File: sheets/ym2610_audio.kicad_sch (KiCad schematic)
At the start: 55 parts, among them J3 SMK S-G8043, Q101 2SC1815, Q102 2SC1815, U26 YM3016D, U27 YM2610, U28 PC4741, U29 PC4741

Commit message: Sync footprints from Nightly Build
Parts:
- C11, C12, C2, C301, C4, C5, C6, C7, C8: footprint 1_NeoGeoLibrary:CAP1-5mm -> 1_NeoGeoLibrary:CAP2-2.5mm
- C24, C25: footprint 1_NeoGeoLibrary:CAP3-5mm -> 1_NeoGeoLibrary:CAP2-2.5mm
- Q101, Q102: footprint Package_TO_SOT_THT:TO-92_Inline -> Package_TO_SOT_THT:TO-92_Inline_Wide
- R33, R34: footprint 1_NeoGeoLibrary:Resistor1-5mm -> Resistor_THT:R_Axial_DIN0207_L6.3mm_D2.5mm_P10.16mm_Horizontal
- U27: footprint Package_DIP:DIP-64_W25.4mm -> 1_NeoGeoLibrary:68000
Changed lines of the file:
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@@
     (property "Reference" "C4" (id 0) (at 105.664 221.107 90))
     (property "Value" "10uF" (id 1) (at 105.918 222.885 90))
-    (property "Footprint" "1_NeoGeoLibrary:CAP1-5mm" (id 2) (at 105.791 217.678 0)
+    (property "Footprint" "1_NeoGeoLibrary:CAP2-2.5mm" (id 2) (at 105.791 217.678 0)
       (effects (font (size 1.27 1.27)) hide)
     )
@@
       (effects (font (size 1.27 1.27)) (justify right))
     )
-    (property "Footprint" "1_NeoGeoLibrary:CAP3-5mm" (id 2) (at 58.928 239.522 0)
+    (property "Footprint" "1_NeoGeoLibrary:CAP2-2.5mm" (id 2) (at 58.928 239.522 0)
       (effects (font (size 1.27 1.27)) hide)
     )
@@
       (effects (font (size 1.27 1.27)) (justify left))
     )
-    (property "Footprint" "Package_TO_SOT_THT:TO-92_Inline" (id 2) (at 185.293 210.058 0)
+    (property "Footprint" "Package_TO_SOT_THT:TO-92_Inline_Wide" (id 2) (at 185.293 210.058 0)
       (effects (font (size 1.27 1.27) italic) (justify left) hide)
     )
@@
       (effects (font (size 1.27 1.27)) (justify left))
     )
-    (property "Footprint" "Package_TO_SOT_THT:TO-92_Inline" (id 2) (at 185.293 225.298 0)
+    (property "Footprint" "Package_TO_SOT_THT:TO-92_Inline_Wide" (id 2) (at 185.293 225.298 0)
       (effects (font (size 1.27 1.27) italic) (justify left) hide)
     )
@@
     (property "Reference" "C8" (id 0) (at 232.029 232.918 90))
     (property "Value" "10uF" (id 1) (at 232.029 234.696 90))
-    (property "Footprint" "1_NeoGeoLibrary:CAP1-5mm" (id 2) (at 232.029 230.378 0)
+    (property "Footprint" "1_NeoGeoLibrary:CAP2-2.5mm" (id 2) (at 232.029 230.378 0)
       (effects (font (size 1.27 1.27)) hide)
     )
@@
       (effects (font (size 1.27 1.27)) (justify left))
     )
-    (property "Footprint" "1_NeoGeoLibrary:CAP1-5mm" (id 2) (at 186.182 56.261 0)
+    (property "Footprint" "1_NeoGeoLibrary:CAP2-2.5mm" (id 2) (at 186.182 56.261 0)
       (effects (font (size 1.27 1.27)) hide)
     )
@@
     (property "Reference" "R33" (id 0) (at 239.776 221.869 90))
     (property "Value" "10Ω" (id 1) (at 239.776 224.409 90))
-    (property "Footprint" "1_NeoGeoLibrary:Resistor1-5mm" (id 2) (at 239.776 226.568 0)
+    (property "Footprint" "Resistor_THT:R_Axial_DIN0207_L6.3mm_D2.5mm_P10.16mm_Horizontal" (id 2) (at 239.776 226.568 0)
       (effects (font (size 1.27 1.27)) hide)
     )
@@
     (property "Reference" "C11" (id 0) (at 117.094 252.73 90))
     (property "Value" "10uF" (id 1) (at 117.348 254.508 90))
-    (property "Footprint" "1_NeoGeoLibrary:CAP1-5mm" (id 2) (at 117.221 249.301 0)
+    (property "Footprint" "1_NeoGeoLibrary:CAP2-2.5mm" (id 2) (at 117.221 249.301 0)
       (effects (font (size 1.27 1.27)) hide)
     )
@@
     (property "Reference" "R34" (id 0) (at 239.776 213.487 90))
     (property "Value" "10Ω" (id 1) (at 239.776 210.947 90))
-    (property "Footprint" "1_NeoGeoLibrary:Resistor1-5mm" (id 2) (at 239.776 208.788 0)
+    (property "Footprint" "Resistor_THT:R_Axial_DIN0207_L6.3mm_D2.5mm_P10.16mm_Horizontal" (id 2) (at 239.776 208.788 0)
       (effects (font (size 1.27 1.27)) hide)
     )
@@
     (property "Reference" "C12" (id 0) (at 117.221 181.102 90))
     (property "Value" "10uF" (id 1) (at 117.221 183.134 90))
-    (property "Footprint" "1_NeoGeoLibrary:CAP1-5mm" (id 2) (at 117.221 186.055 0)
+    (property "Footprint" "1_NeoGeoLibrary:CAP2-2.5mm" (id 2) (at 117.221 186.055 0)
       (effects (font (size 1.27 1.27)) hide)
     )
@@
     (property "Reference" "C5" (id 0) (at 186.944 197.231 0))
     (property "Value" "10uF" (id 1) (at 187.071 199.009 0))
-    (property "Footprint" "1_NeoGeoLibrary:CAP1-5mm" (id 2) (at 182.753 197.993 0)
+    (property "Footprint" "1_NeoGeoLibrary:CAP2-2.5mm" (id 2) (at 182.753 197.993 0)
       (effects (font (size 1.27 1.27)) hide)
     )
@@
       (effects (font (size 1.27 1.27)) (justify right))
     )
-    (property "Footprint" "1_NeoGeoLibrary:CAP1-5mm" (id 2) (at 233.426 50.546 0)
+    (property "Footprint" "1_NeoGeoLibrary:CAP2-2.5mm" (id 2) (at 233.426 50.546 0)
       (effects (font (size 1.27 1.27)) hide)
     )
@@
     (property "Reference" "C6" (id 0) (at 187.198 236.474 0))
     (property "Value" "10uF" (id 1) (at 187.198 238.252 0))
-    (property "Footprint" "1_NeoGeoLibrary:CAP1-5mm" (id 2) (at 182.753 237.363 0)
+    (property "Footprint" "1_NeoGeoLibrary:CAP2-2.5mm" (id 2) (at 182.753 237.363 0)
       (effects (font (size 1.27 1.27)) hide)
     )
@@
     (property "Reference" "U27" (id 0) (at 100.33 29.845 0))
     (property "Value" "YM2610" (id 1) (at 108.458 138.811 0))
-    (property "Footprint" "Package_DIP:DIP-64_W25.4mm" (id 2) (at 108.458 89.281 0)
+    (property "Footprint" "1_NeoGeoLibrary:68000" (id 2) (at 108.458 89.281 0)
       (effects (font (size 1.27 1.27)) hide)
     )
@@
     (property "Reference" "C7" (id 0) (at 232.029 200.66 90))
     (property "Value" "10uF" (id 1) (at 232.029 202.438 90))
-    (property "Footprint" "1_NeoGeoLibrary:CAP1-5mm" (id 2) (at 232.029 204.978 0)
+    (property "Footprint" "1_NeoGeoLibrary:CAP2-2.5mm" (id 2) (at 232.029 204.978 0)
       (effects (font (size 1.27 1.27)) hide)
     )
@@
       (effects (font (size 1.27 1.27)) (justify right))
     )
-    (property "Footprint" "1_NeoGeoLibrary:CAP3-5mm" (id 2) (at 58.928 195.834 0)
-      (effects (font (size 1.27 1.27)) hide)
-    )
+    (property "Footprint" "1_NeoGeoLibrary:CAP2-2.5mm" (id 2) (at 58.928 195.834 0)
+      (effects (font (size 1.27 1.27)) hide)
+    )

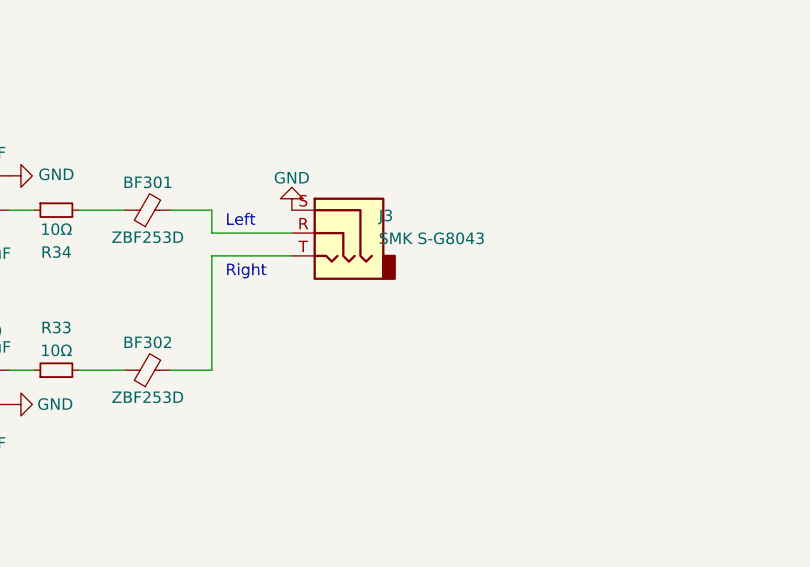
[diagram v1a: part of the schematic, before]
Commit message: 1. Swap Halt / Reset on RA1 2. Added more Power Caps 3. Change Audio socket Left/Right around 4. Added Ferrite Beads to Audio Signals 5. Added Ferrite Beads to Video Signals
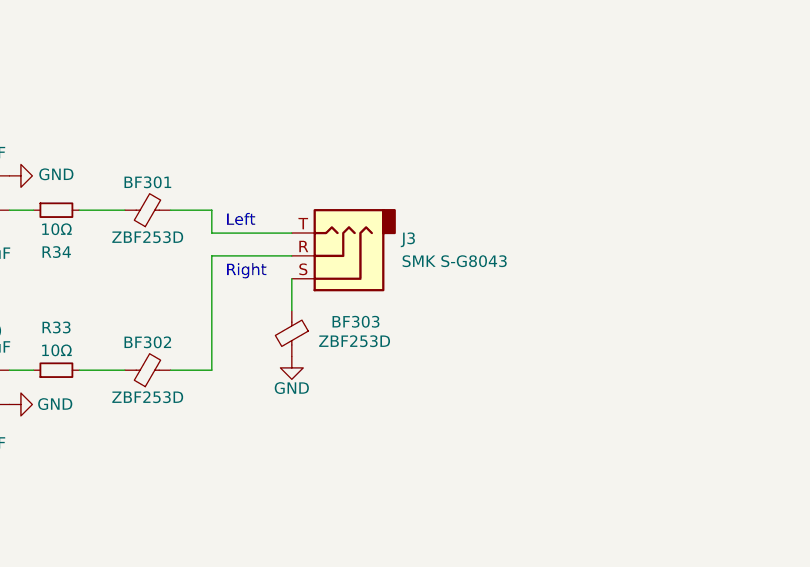
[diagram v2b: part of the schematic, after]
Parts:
- added BF303: ZBF253D, 1_NeoGeoLibrary:BF-2.5mm, symbol Device:FerriteBead_Small
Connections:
- net GND: now also BF303.2; no longer J3.S
- net at BF301.2: now also J3.T; no longer J3.R
- net at BF302.2: now also J3.R; no longer J3.T
- new net: BF303.1, J3.S
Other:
- moved on the sheet: J3
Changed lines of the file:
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@@
+    (stroke (width 0) (type default) (color 0 0 0 0))
+  )
+  (wire (pts (xy 265.938 216.408) (xy 265.938 219.964))
     (stroke (width 0) (type default) (color 0 0 0 0))
   )
@@
     (pin "2")
   )
+  (symbol (lib_id "Device:FerriteBead_Small") (at 265.938 222.504 0) (mirror y) (unit 1)
+    (in_bom yes) (on_board yes)
+    (property "Reference" "BF303" (id 0) (at 273.05 221.234 0))
+    (property "Value" "ZBF253D" (id 1) (at 272.923 223.393 0))
+    (property "Footprint" "1_NeoGeoLibrary:BF-2.5mm" (id 2) (at 267.716 222.504 90)
+      (effects (font (size 1.27 1.27)) hide)
+    )
+    (property "Datasheet" "" (id 3) (at 265.938 222.504 0)
+      (effects (font (size 1.27 1.27)) hide)
+    )
+    (pin "1")
+    (pin "2")
+  )
   (symbol (lib_id "Device:R_Small") (at 222.885 206.883 270) (mirror x) (unit 1)
     (in_bom yes) (on_board yes)
@@
     (pin "2")
   )
-  (symbol (lib_id "power:GND") (at 265.938 208.788 180) (unit 1)
-    (in_bom yes) (on_board yes)
-    (property "Reference" "#PWR0193" (id 0) (at 265.938 202.438 0)
-      (effects (font (size 1.27 1.27)) hide)
-    )
-    (property "Value" "GND" (id 1) (at 265.938 205.232 0))
-    (property "Footprint" "" (id 2) (at 265.938 208.788 0)
-      (effects (font (size 1.27 1.27)) hide)
-    )
-    (property "Datasheet" "" (id 3) (at 265.938 208.788 0)
+  (symbol (lib_id "power:GND") (at 265.938 225.044 0) (mirror y) (unit 1)
+    (in_bom yes) (on_board yes)
+    (property "Reference" "#PWR0193" (id 0) (at 265.938 231.394 0)
+      (effects (font (size 1.27 1.27)) hide)
+    )
+    (property "Value" "GND" (id 1) (at 265.938 228.6 0))
+    (property "Footprint" "" (id 2) (at 265.938 225.044 0)
+      (effects (font (size 1.27 1.27)) hide)
+    )
+    (property "Datasheet" "" (id 3) (at 265.938 225.044 0)
       (effects (font (size 1.27 1.27)) hide)
     )
@@
   (symbol (lib_id "power:GND") (at 58.928 252.095 0) (unit 1)
     (in_bom yes) (on_board yes)
-    (property "Reference" "#PWR?" (id 0) (at 58.928 258.445 0)
+    (property "Reference" "#PWR0199" (id 0) (at 58.928 258.445 0)
       (effects (font (size 1.27 1.27)) hide)
     )
@@
     (pin "2")
   )
-  (symbol (lib_id "Connector:AudioJack3") (at 271.018 211.328 0) (mirror y) (unit 1)
+  (symbol (lib_id "Connector:AudioJack3") (at 271.018 213.868 180) (unit 1)
     (in_bom yes) (on_board yes) (fields_autoplaced)
-    (property "Reference" "J3" (id 0) (at 275.59 209.4229 0)
+    (property "Reference" "J3" (id 0) (at 278.13 211.9629 0)
       (effects (font (size 1.27 1.27)) (justify right))
     )
-    (property "Value" "SMK S-G8043" (id 1) (at 275.59 211.9629 0)
+    (property "Value" "SMK S-G8043" (id 1) (at 278.13 214.5029 0)
       (effects (font (size 1.27 1.27)) (justify right))
     )
-    (property "Footprint" "Connector_Audio:Jack_3.5mm_CUI_SJ1-3523N_Horizontal" (id 2) (at 271.018 211.328 0)
-      (effects (font (size 1.27 1.27)) hide)
-    )
-    (property "Datasheet" "~" (id 3) (at 271.018 211.328 0)
+    (property "Footprint" "Connector_Audio:Jack_3.5mm_CUI_SJ1-3523N_Horizontal" (id 2) (at 271.018 213.868 0)
+      (effects (font (size 1.27 1.27)) hide)
+    )
+    (property "Datasheet" "~" (id 3) (at 271.018 213.868 0)
       (effects (font (size 1.27 1.27)) hide)
     )
@@
   (symbol (lib_id "power:GND") (at 58.928 183.261 180) (unit 1)
     (in_bom yes) (on_board yes)
-    (property "Reference" "#PWR?" (id 0) (at 58.928 176.911 0)
-      (effects (font (size 1.27 1.27)) hide)
-    )
+    (property "Reference" "#PWR0200" (id 0) (at 58.928 176.911 0)
+      (effects (font (size 1.27 1.27)) hide)
+    )

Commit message: Sync Footprints from Nightly
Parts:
- J3: footprint Connector_Audio:Jack_3.5mm_CUI_SJ1-3523N_Horizontal -> 1_NeoGeoLibrary:J3
- Q101, Q102: footprint Package_TO_SOT_THT:TO-92_Inline_Wide -> 1_NeoGeoLibrary:Transistor
- RV1: footprint Connector_PinHeader_2.54mm:PinHeader_1x06_P2.54mm_Vertical -> 1_NeoGeoLibrary:Volume-Slider
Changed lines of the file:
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@@
       (effects (font (size 1.27 1.27)) (justify left))
     )
-    (property "Footprint" "Package_TO_SOT_THT:TO-92_Inline_Wide" (id 2) (at 185.293 210.058 0)
+    (property "Footprint" "1_NeoGeoLibrary:Transistor" (id 2) (at 185.293 210.058 0)
       (effects (font (size 1.27 1.27) italic) (justify left) hide)
     )
@@
       (effects (font (size 1.27 1.27)) (justify left))
     )
-    (property "Footprint" "Package_TO_SOT_THT:TO-92_Inline_Wide" (id 2) (at 185.293 225.298 0)
+    (property "Footprint" "1_NeoGeoLibrary:Transistor" (id 2) (at 185.293 225.298 0)
       (effects (font (size 1.27 1.27) italic) (justify left) hide)
     )
@@
       (effects (font (size 1.27 1.27)) (justify right))
     )
-    (property "Footprint" "Connector_PinHeader_2.54mm:PinHeader_1x06_P2.54mm_Vertical" (id 2) (at 59.563 211.328 0)
+    (property "Footprint" "1_NeoGeoLibrary:Volume-Slider" (id 2) (at 59.563 211.328 0)
       (effects (font (size 1.27 1.27)) hide)
     )
@@
       (effects (font (size 1.27 1.27)) (justify right))
     )
-    (property "Footprint" "Connector_Audio:Jack_3.5mm_CUI_SJ1-3523N_Horizontal" (id 2) (at 271.018 213.868 0)
-      (effects (font (size 1.27 1.27)) hide)
-    )
+    (property "Footprint" "1_NeoGeoLibrary:J3" (id 2) (at 271.018 213.868 0)
+      (effects (font (size 1.27 1.27)) hide)
+    )

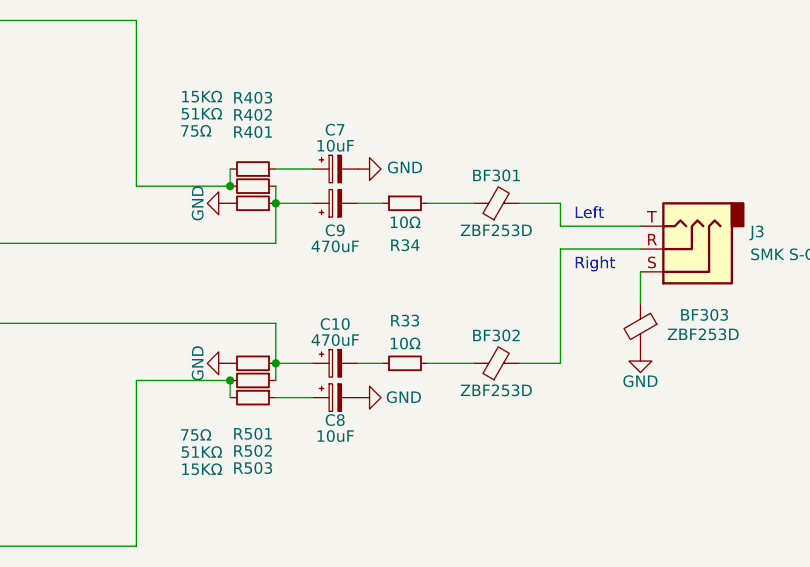
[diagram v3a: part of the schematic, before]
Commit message: Swapped Audio Resistors Around
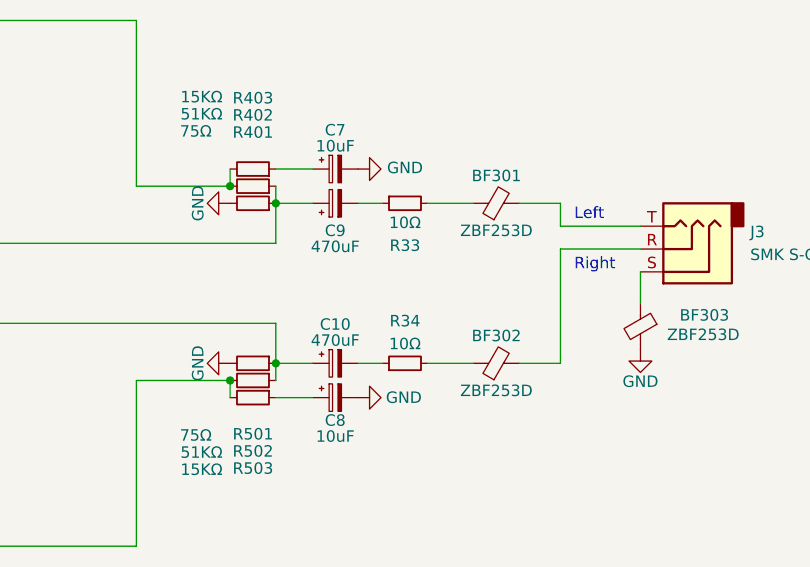
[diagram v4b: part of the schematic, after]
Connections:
- net at C9.2: now also R33.1; no longer R34.1
- net at BF301.1: now also R33.2; no longer R34.2
- net at C10.2: now also R34.1; no longer R33.1
- net at BF302.1: now also R34.2; no longer R33.2
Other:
- moved on the sheet: R33, R34
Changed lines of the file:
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@@
     (pin "1")
   )
-  (symbol (lib_id "Device:R_Small") (at 239.776 226.568 90) (unit 1)
+  (symbol (lib_id "Device:R_Small") (at 239.776 208.788 90) (mirror x) (unit 1)
     (in_bom yes) (on_board yes)
-    (property "Reference" "R33" (id 0) (at 239.776 221.869 90))
-    (property "Value" "10Ω" (id 1) (at 239.776 224.409 90))
-    (property "Footprint" "Resistor_THT:R_Axial_DIN0207_L6.3mm_D2.5mm_P10.16mm_Horizontal" (id 2) (at 239.776 226.568 0)
+    (property "Reference" "R33" (id 0) (at 239.776 213.487 90))
+    (property "Value" "10Ω" (id 1) (at 239.776 210.947 90))
+    (property "Footprint" "Resistor_THT:R_Axial_DIN0207_L6.3mm_D2.5mm_P10.16mm_Horizontal" (id 2) (at 239.776 208.788 0)
       (effects (font (size 1.27 1.27)) hide)
     )
-    (property "Datasheet" "" (id 3) (at 239.776 226.568 0)
+    (property "Datasheet" "" (id 3) (at 239.776 208.788 0)
       (effects (font (size 1.27 1.27)) hide)
     )
@@
     (pin "2")
   )
-  (symbol (lib_id "Device:R_Small") (at 239.776 208.788 90) (mirror x) (unit 1)
+  (symbol (lib_id "Device:R_Small") (at 239.776 226.568 90) (unit 1)
     (in_bom yes) (on_board yes)
-    (property "Reference" "R34" (id 0) (at 239.776 213.487 90))
-    (property "Value" "10Ω" (id 1) (at 239.776 210.947 90))
-    (property "Footprint" "Resistor_THT:R_Axial_DIN0207_L6.3mm_D2.5mm_P10.16mm_Horizontal" (id 2) (at 239.776 208.788 0)
+    (property "Reference" "R34" (id 0) (at 239.776 221.869 90))
+    (property "Value" "10Ω" (id 1) (at 239.776 224.409 90))
+    (property "Footprint" "Resistor_THT:R_Axial_DIN0207_L6.3mm_D2.5mm_P10.16mm_Horizontal" (id 2) (at 239.776 226.568 0)
       (effects (font (size 1.27 1.27)) hide)
     )
-    (property "Datasheet" "" (id 3) (at 239.776 208.788 0)
+    (property "Datasheet" "" (id 3) (at 239.776 226.568 0)
       (effects (font (size 1.27 1.27)) hide)
     )
